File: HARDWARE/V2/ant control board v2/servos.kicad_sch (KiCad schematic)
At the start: 2 parts, among them J6 servo 1, J7 servo 2

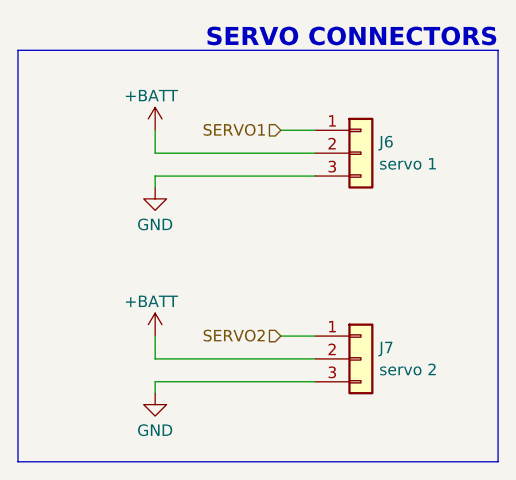
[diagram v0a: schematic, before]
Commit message: layout 2.0 facv2 done
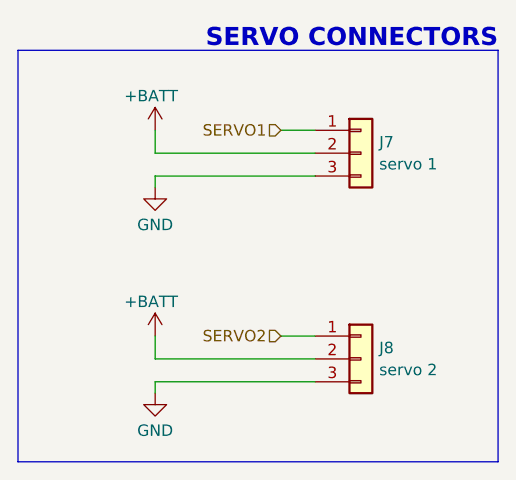
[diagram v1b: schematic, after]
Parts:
- J7: renamed from J6; footprint _MY_connectors:Pad 03x01 -> _MY_connectors:01x03_TH_pad_renforced
- J8: renamed from J7; footprint _MY_connectors:Pad 03x01 -> _MY_connectors:01x03_TH_pad_renforced
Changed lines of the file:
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@@
 	(title_block
 		(title "Ant Robot control board")
-		(date "2025-05-05")
+		(date "2025-09-18")
 		(rev "2.0")
 		(company "Filippo Castellan")
@@
 		(dnp no)
 		(fields_autoplaced yes)
-		(property "Reference" "J6"
+		(property "Reference" "J7"
 			(at 150.622 82.5972 0)
 			(effects
@@
 			)
 		)
-		(property "Footprint" "_MY_connectors:Pad 03x01"
+		(property "Footprint" "_MY_connectors:01x03_TH_pad_renforced"
 			(at 148.59 83.82 0)
 			(effects
@@
 			(project "ant control board v2"
 				(path "/53484dc5-354c-4967-b00e-d73de62a4245/11638847-2904-4dcc-b1cc-a24fa7661082"
-					(reference "J6")
+					(reference "J7")
 					(unit 1)
 				)
@@
 		(on_board yes)
 		(dnp no)
-		(property "Reference" "#PWR035"
+		(property "Reference" "#PWR022"
 			(at 125.73 85.09 0)
 			(effects
@@
 			(project "ant control board v2"
 				(path "/53484dc5-354c-4967-b00e-d73de62a4245/11638847-2904-4dcc-b1cc-a24fa7661082"
-					(reference "#PWR035")
+					(reference "#PWR022")
 					(unit 1)
 				)
@@
 		(on_board yes)
 		(dnp no)
-		(property "Reference" "#PWR036"
+		(property "Reference" "#PWR023"
 			(at 125.73 93.98 0)
 			(effects
@@
 			(project "ant control board v2"
 				(path "/53484dc5-354c-4967-b00e-d73de62a4245/11638847-2904-4dcc-b1cc-a24fa7661082"
-					(reference "#PWR036")
+					(reference "#PWR023")
 					(unit 1)
 				)
@@
 		(on_board yes)
 		(dnp no)
-		(property "Reference" "#PWR038"
+		(property "Reference" "#PWR025"
 			(at 125.73 116.84 0)
 			(effects
@@
 			(project "ant control board v2"
 				(path "/53484dc5-354c-4967-b00e-d73de62a4245/11638847-2904-4dcc-b1cc-a24fa7661082"
-					(reference "#PWR038")
+					(reference "#PWR025")
 					(unit 1)
 				)
@@
 		(on_board yes)
 		(dnp no)
-		(property "Reference" "#PWR037"
+		(property "Reference" "#PWR024"
 			(at 125.73 107.95 0)
 			(effects
@@
 			(project "ant control board v2"
 				(path "/53484dc5-354c-4967-b00e-d73de62a4245/11638847-2904-4dcc-b1cc-a24fa7661082"
-					(reference "#PWR037")
+					(reference "#PWR024")
 					(unit 1)
 				)
@@
 		(dnp no)
 		(fields_autoplaced yes)
-		(property "Reference" "J7"
+		(property "Reference" "J8"
 			(at 150.622 105.4572 0)
 			(effects
@@
 			)
 		)
-		(property "Footprint" "_MY_connectors:Pad 03x01"
+		(property "Footprint" "_MY_connectors:01x03_TH_pad_renforced"
 			(at 148.59 106.68 0)
 			(effects
@@
 			(project "ant control board v2"
 				(path "/53484dc5-354c-4967-b00e-d73de62a4245/11638847-2904-4dcc-b1cc-a24fa7661082"
-					(reference "J7")
+					(reference "J8")
 					(unit 1)
 				)
